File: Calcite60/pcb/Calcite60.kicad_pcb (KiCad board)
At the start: 2 copper layers, 226 x 94.8 mm, 176 parts, among them J1 USB_C_Receptacle_USB2.0, SW1 BOOT, SW2 RESET, U1 RT9013-33GB, U2 SRV05-4, U3 W25Q128JVS, U4 RP2040, Y1 12MHz

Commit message: Update BOM
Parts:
- renumbered H8 to H1, H3 to H10, H5 to H11, H1 to H12, H2 to H13, H14 to H2, H13 to H3, H12 to H4, H11 to H5, H9 to H6, H10 to H7, H4 to H8, H6 to H9

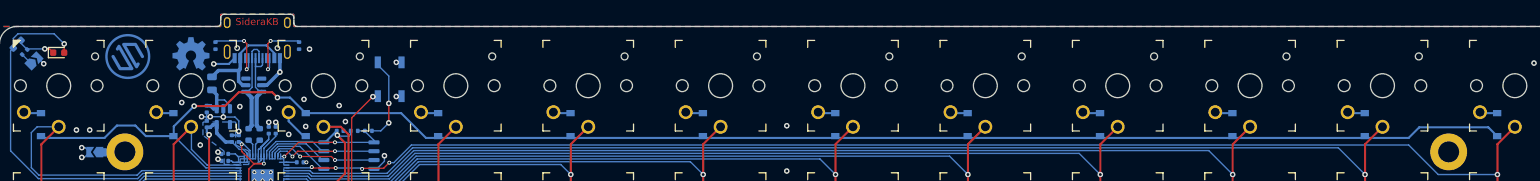
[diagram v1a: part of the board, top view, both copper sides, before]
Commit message: Reduce the size of the USB protrusion
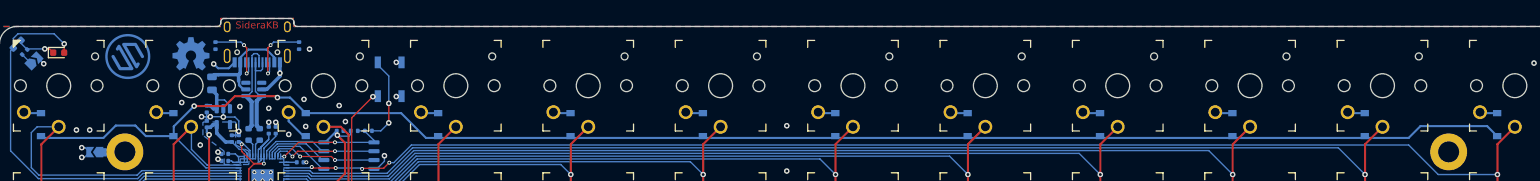
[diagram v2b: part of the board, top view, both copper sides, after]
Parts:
- moved J1 0.60 mm to (69.1, 50.5)
- moved U2 0.60 mm to (68.6, 58.4)
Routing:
- net /USB_D+: track 14.4 -> 13.8 mm
- net /USB_D-: track 14.3 -> 13.7 mm
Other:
- board size 226 x 94.8 mm -> 226 x 94.2 mm

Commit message: Update Calcite60 Rev2
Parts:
- removed C10, C11, C12, C13, C14, C15, C9: 100nF, Capacitor_SMD:C_0402_1005Metric
- removed C16, C8: 1uF, Capacitor_SMD:C_0402_1005Metric
- removed the SB1 at (37.1, 54.4)
- removed the U2 at (68.6, 58.4)
- added D1: 1N5819, Diode_SMD:D_SOD-323_HandSoldering, B.Cu at (43.7, 89.9)
- added H14: MountingHole, calcite:MountingWuerth_M2, B.Cu at (202.1, 67.4)
- added H15: MountingHole, calcite:MountingWuerth_M2, B.Cu at (240.1, 86.4)
- added H16: MountingHole, calcite:MountingWuerth_M2, B.Cu at (88.1, 67.4)
- added H17: MountingHole, calcite:MountingWuerth_M2, B.Cu at (50.1, 86.4)
- added H18: MountingHole, calcite:mouse_bite, F.Cu at (220.6, 123.7)
- added H19: MountingHole, calcite:mouse_bite, F.Cu at (220.6, 126.2)
- added H20: MountingHole, calcite:mouse_bite, F.Cu at (69.6, 123.7)
- added H21: MountingHole, calcite:mouse_bite, F.Cu at (69.6, 126.2)
- added H22: MountingHole, calcite:mouse_bite, F.Cu at (127.6, 123.7)
- added H23: MountingHole, calcite:mouse_bite, F.Cu at (127.6, 126.2)
- added H24: MountingHole, calcite:mouse_bite, F.Cu at (162.6, 123.7)
- added H25: MountingHole, calcite:mouse_bite, F.Cu at (162.6, 126.2)
- added J2: Conn_01x02, Connector_PinHeader_2.54mm:PinHeader_1x02_P2.54mm_Vertical, B.Cu at (150.6, 81.6)
- added J3: Conn_01x02, Connector_JST:JST_PH_S2B-PH-K_1x02_P2.00mm_Horizontal, B.Cu at (154.7, 81.9)
- added J4: Conn_01x02, Connector_PinHeader_2.54mm:PinHeader_1x02_P2.54mm_Vertical, B.Cu at (139.6, 84.2)
- added J5: Conn_01x02, Connector_JST:JST_PH_S2B-PH-K_1x02_P2.00mm_Horizontal, B.Cu at (135.6, 83.9)
- added J6: Conn_01x04, Connector_PinHeader_2.54mm:PinHeader_1x04_P2.54mm_Vertical, B.Cu at (110.1, 51.4)
- added J7: Conn_02x05_Counter_Clockwise, Connector_PinHeader_1.27mm:PinHeader_2x05_P1.27mm_Vertical, B.Cu at (122.1, 51.3)
- added KEY64: SW_Push_45deg, key-switches:SW_Kailh_Choc_V1_THT_nSilk, F.Cu at (126.1, 114.9)
- added KEY65: SW_Push_45deg, key-switches:SW_Kailh_Choc_V1_THT_nSilk, F.Cu at (145.1, 114.9)
- added KEY66: SW_Push_45deg, key-switches:SW_Kailh_Choc_V1_THT_nSilk, F.Cu at (164.1, 114.9)
- added LD1: Blue, LED_SMD:LED_0603_1608Metric, B.Cu at (61.6, 50.7)
- added Q1: AO3407, Package_TO_SOT_SMD:SOT-23, B.Cu at (43.6, 86.4)
- added R10: 820k, Resistor_SMD:R_0603_1608Metric, B.Cu at (60.6, 88.7)
- added U1: SRV05-4, Package_TO_SOT_SMD:SOT-23-6, B.Cu at (69.1, 58.9)
- C1: renamed from C3; value 100nF -> 1uF; footprint Capacitor_SMD:C_0402_1005Metric -> Capacitor_SMD:C_0603_1608Metric
- C2: renamed from C1; footprint Capacitor_SMD:C_0402_1005Metric -> Capacitor_SMD:C_0603_1608Metric
- C3: renamed from C2; footprint Capacitor_SMD:C_0402_1005Metric -> Capacitor_SMD:C_0603_1608Metric
- C4, C5: value 20pF -> 12pF; footprint Capacitor_SMD:C_0402_1005Metric -> Capacitor_SMD:C_0603_1608Metric
- C6, C7: value 100nF -> 10uF; footprint Capacitor_SMD:C_0402_1005Metric -> Capacitor_SMD:C_0603_1608Metric
- KEY1, KEY63: footprint key-switches:SW_Kailh_Choc_V1_THT -> key-switches:SW_Kailh_Choc_V1_THT_nSilk
- KEY10: renamed from KEY50; footprint key-switches:SW_Kailh_Choc_V1_THT -> key-switches:SW_Kailh_Choc_V1_THT_nSilk
- KEY11: renamed from KEY3; footprint key-switches:SW_Kailh_Choc_V1_THT -> key-switches:SW_Kailh_Choc_V1_THT_nSilk
- KEY12: renamed from KEY15; footprint key-switches:SW_Kailh_Choc_V1_THT -> key-switches:SW_Kailh_Choc_V1_THT_nSilk
- KEY13: renamed from KEY27; footprint key-switches:SW_Kailh_Choc_V1_THT -> key-switches:SW_Kailh_Choc_V1_THT_nSilk
- KEY14: renamed from KEY39; footprint key-switches:SW_Kailh_Choc_V1_THT -> key-switches:SW_Kailh_Choc_V1_THT_nSilk
- KEY15: renamed from KEY51; footprint key-switches:SW_Kailh_Choc_V1_THT -> key-switches:SW_Kailh_Choc_V1_THT_nSilk
- KEY16: renamed from KEY4; footprint key-switches:SW_Kailh_Choc_V1_THT -> key-switches:SW_Kailh_Choc_V1_THT_nSilk
- KEY17: renamed from KEY16; footprint key-switches:SW_Kailh_Choc_V1_THT -> key-switches:SW_Kailh_Choc_V1_THT_nSilk
- KEY18: renamed from KEY28; footprint key-switches:SW_Kailh_Choc_V1_THT -> key-switches:SW_Kailh_Choc_V1_THT_nSilk
- KEY19: renamed from KEY40; footprint key-switches:SW_Kailh_Choc_V1_THT -> key-switches:SW_Kailh_Choc_V1_THT_nSilk
- KEY2: renamed from KEY13; footprint key-switches:SW_Kailh_Choc_V1_THT -> key-switches:SW_Kailh_Choc_V1_THT_nSilk
- KEY20: renamed from KEY52; footprint key-switches:SW_Kailh_Choc_V1_THT -> key-switches:SW_Kailh_Choc_V1_THT_nSilk
- KEY21: renamed from KEY53; footprint key-switches:SW_Kailh_Choc_V1_THT -> key-switches:SW_Kailh_Choc_V1_THT_nSilk
- KEY22: renamed from KEY5; footprint key-switches:SW_Kailh_Choc_V1_THT -> key-switches:SW_Kailh_Choc_V1_THT_nSilk
- KEY23: renamed from KEY17; footprint key-switches:SW_Kailh_Choc_V1_THT -> key-switches:SW_Kailh_Choc_V1_THT_nSilk
- KEY24: renamed from KEY29; footprint key-switches:SW_Kailh_Choc_V1_THT -> key-switches:SW_Kailh_Choc_V1_THT_nSilk
- KEY25: renamed from KEY41; footprint key-switches:SW_Kailh_Choc_V1_THT -> key-switches:SW_Kailh_Choc_V1_THT_nSilk
- KEY26: renamed from KEY54; footprint key-switches:SW_Kailh_Choc_V1_THT -> key-switches:SW_Kailh_Choc_V1_THT_nSilk
- KEY27: renamed from KEY6; footprint key-switches:SW_Kailh_Choc_V1_THT -> key-switches:SW_Kailh_Choc_V1_THT_nSilk
- KEY28: renamed from KEY18; footprint key-switches:SW_Kailh_Choc_V1_THT -> key-switches:SW_Kailh_Choc_V1_THT_nSilk
- KEY29: renamed from KEY30; footprint key-switches:SW_Kailh_Choc_V1_THT -> key-switches:SW_Kailh_Choc_V1_THT_nSilk
- KEY3: renamed from KEY25; footprint key-switches:SW_Kailh_Choc_V1_THT -> key-switches:SW_Kailh_Choc_V1_THT_nSilk
- KEY30: renamed from KEY42; footprint key-switches:SW_Kailh_Choc_V1_THT -> key-switches:SW_Kailh_Choc_V1_THT_nSilk
- KEY31: renamed from KEY55; footprint key-switches:SW_Kailh_Choc_V1_THT -> key-switches:SW_Kailh_Choc_V1_THT_nSilk
- KEY32: renamed from KEY56; footprint key-switches:SW_Kailh_Choc_V1_THT -> key-switches:SW_Kailh_Choc_V1_THT_nSilk
- KEY33: renamed from KEY7; footprint key-switches:SW_Kailh_Choc_V1_THT -> key-switches:SW_Kailh_Choc_V1_THT_nSilk
- KEY34: renamed from KEY19; footprint key-switches:SW_Kailh_Choc_V1_THT -> key-switches:SW_Kailh_Choc_V1_THT_nSilk
- KEY35: renamed from KEY31; footprint key-switches:SW_Kailh_Choc_V1_THT -> key-switches:SW_Kailh_Choc_V1_THT_nSilk
- KEY36: renamed from KEY43; footprint key-switches:SW_Kailh_Choc_V1_THT -> key-switches:SW_Kailh_Choc_V1_THT_nSilk
- KEY37: renamed from KEY57; footprint key-switches:SW_Kailh_Choc_V1_THT -> key-switches:SW_Kailh_Choc_V1_THT_nSilk
- KEY38: renamed from KEY58; footprint key-switches:SW_Kailh_Choc_V1_THT -> key-switches:SW_Kailh_Choc_V1_THT_nSilk
- KEY39: renamed from KEY8; footprint key-switches:SW_Kailh_Choc_V1_THT -> key-switches:SW_Kailh_Choc_V1_THT_nSilk
- KEY4: renamed from KEY37; footprint key-switches:SW_Kailh_Choc_V1_THT -> key-switches:SW_Kailh_Choc_V1_THT_nSilk
- KEY40: renamed from KEY20; footprint key-switches:SW_Kailh_Choc_V1_THT -> key-switches:SW_Kailh_Choc_V1_THT_nSilk
- KEY41: renamed from KEY32; footprint key-switches:SW_Kailh_Choc_V1_THT -> key-switches:SW_Kailh_Choc_V1_THT_nSilk
- KEY42: renamed from KEY44; footprint key-switches:SW_Kailh_Choc_V1_THT -> key-switches:SW_Kailh_Choc_V1_THT_nSilk
- KEY43: renamed from KEY59; footprint key-switches:SW_Kailh_Choc_V1_THT -> key-switches:SW_Kailh_Choc_V1_THT_nSilk
- KEY44: renamed from KEY9; footprint key-switches:SW_Kailh_Choc_V1_THT -> key-switches:SW_Kailh_Choc_V1_THT_nSilk
- KEY45: renamed from KEY21; footprint key-switches:SW_Kailh_Choc_V1_THT -> key-switches:SW_Kailh_Choc_V1_THT_nSilk
- KEY46: renamed from KEY33; footprint key-switches:SW_Kailh_Choc_V1_THT -> key-switches:SW_Kailh_Choc_V1_THT_nSilk
- KEY47: renamed from KEY45; footprint key-switches:SW_Kailh_Choc_V1_THT -> key-switches:SW_Kailh_Choc_V1_THT_nSilk
- KEY48: renamed from KEY60; footprint key-switches:SW_Kailh_Choc_V1_THT -> key-switches:SW_Kailh_Choc_V1_THT_nSilk
- KEY49: renamed from KEY10; footprint key-switches:SW_Kailh_Choc_V1_THT -> key-switches:SW_Kailh_Choc_V1_THT_nSilk
- KEY5: renamed from KEY49; footprint key-switches:SW_Kailh_Choc_V1_THT -> key-switches:SW_Kailh_Choc_V1_THT_nSilk
- KEY50: renamed from KEY22; footprint key-switches:SW_Kailh_Choc_V1_THT -> key-switches:SW_Kailh_Choc_V1_THT_nSilk
- KEY51: renamed from KEY34; footprint key-switches:SW_Kailh_Choc_V1_THT -> key-switches:SW_Kailh_Choc_V1_THT_nSilk
- KEY52: renamed from KEY46; footprint key-switches:SW_Kailh_Choc_V1_THT -> key-switches:SW_Kailh_Choc_V1_THT_nSilk
- KEY53: renamed from KEY61; footprint key-switches:SW_Kailh_Choc_V1_THT -> key-switches:SW_Kailh_Choc_V1_THT_nSilk
- KEY54: renamed from KEY11; footprint key-switches:SW_Kailh_Choc_V1_THT -> key-switches:SW_Kailh_Choc_V1_THT_nSilk
- KEY55: renamed from KEY23; footprint key-switches:SW_Kailh_Choc_V1_THT -> key-switches:SW_Kailh_Choc_V1_THT_nSilk
- KEY56: renamed from KEY35; footprint key-switches:SW_Kailh_Choc_V1_THT -> key-switches:SW_Kailh_Choc_V1_THT_nSilk
- KEY57: renamed from KEY47; footprint key-switches:SW_Kailh_Choc_V1_THT -> key-switches:SW_Kailh_Choc_V1_THT_nSilk
- KEY58: renamed from KEY62; footprint key-switches:SW_Kailh_Choc_V1_THT -> key-switches:SW_Kailh_Choc_V1_THT_nSilk
- KEY59: renamed from KEY12; footprint key-switches:SW_Kailh_Choc_V1_THT -> key-switches:SW_Kailh_Choc_V1_THT_nSilk
- KEY6: renamed from KEY2; footprint key-switches:SW_Kailh_Choc_V1_THT -> key-switches:SW_Kailh_Choc_V1_THT_nSilk
- KEY60: renamed from KEY24; footprint key-switches:SW_Kailh_Choc_V1_THT -> key-switches:SW_Kailh_Choc_V1_THT_nSilk
- KEY61: renamed from KEY36; footprint key-switches:SW_Kailh_Choc_V1_THT -> key-switches:SW_Kailh_Choc_V1_THT_nSilk
- KEY62: renamed from KEY48; footprint key-switches:SW_Kailh_Choc_V1_THT -> key-switches:SW_Kailh_Choc_V1_THT_nSilk
- KEY7: renamed from KEY14; footprint key-switches:SW_Kailh_Choc_V1_THT -> key-switches:SW_Kailh_Choc_V1_THT_nSilk
- KEY8: renamed from KEY26; footprint key-switches:SW_Kailh_Choc_V1_THT -> key-switches:SW_Kailh_Choc_V1_THT_nSilk
- KEY9: renamed from KEY38; footprint key-switches:SW_Kailh_Choc_V1_THT -> key-switches:SW_Kailh_Choc_V1_THT_nSilk
- LD2: renamed from LD1; moved to F.Cu
- R1, R2, R7, R8: footprint Resistor_SMD:R_0402_1005Metric -> Resistor_SMD:R_0603_1608Metric
- R3: renamed from R4; value 27 -> 1k
- R4: renamed from R5; value 27 -> 5.1k
- R5: renamed from R6; value 1k -> 100k; footprint Resistor_SMD:R_0402_1005Metric -> Resistor_SMD:R_0603_1608Metric
- R6: renamed from R3; footprint Resistor_SMD:R_0402_1005Metric -> Resistor_SMD:R_0603_1608Metric
- R9: value 10k -> 2M; footprint Resistor_SMD:R_0402_1005Metric -> Resistor_SMD:R_0603_1608Metric
- SW1: value BOOT -> SW_DPDT_x2; footprint Button_Switch_SMD:SW_SPST_B3U-1000P -> calcite:9_3.5_3.5 Switch
- U2: renamed from U3; value W25Q128JVS -> TP4054; footprint Package_SO:SOIC-8_5.23x5.23mm_P1.27mm -> Package_TO_SOT_SMD:SOT-23-5
- U4: value RP2040 -> E73-2G4M08S1C; footprint Package_DFN_QFN:QFN-56-1EP_7x7mm_P0.4mm_EP3.2x3.2mm -> calcite:E73-2G4M08S1C-52840
- Y1: value 12MHz -> 32.768kHz; footprint Crystal:Crystal_SMD_3225-4Pin_3.2x2.5mm -> Crystal:Crystal_SMD_3215-2Pin_3.2x1.5mm
- moved G*** 77.8 mm to (143.8, 35.2)
- moved H7 68.5 mm to (183.1, 124.4)
- moved H9 68.5 mm to (107.1, 124.4)
- moved C1 49.5 mm to (38.6, 89.9), turned to 180 degrees
- moved U2 47.4 mm to (38.6, 86.4), turned to -90 degrees
- moved R5 45.3 mm to (43.7, 82.9)
- moved R4 38.8 mm to (35.6, 86.4), turned to 90 degrees
- moved R8 35.8 mm to (43.9, 53.2), turned to -90 degrees
- moved R3 35.7 mm to (38.6, 82.9), turned to 180 degrees
- moved R7 27.5 mm to (60.6, 80.4)
- moved C2 26.8 mm to (56.1, 87.4), turned to 180 degrees
- moved C6 23.6 mm to (60.6, 85.2), turned to 180 degrees
- moved U3 23.0 mm to (56.1, 83.9), turned to 90 degrees
- moved G*** 20.5 mm to (45.0, 34.0)
- moved C4 18.4 mm to (57.6, 92.9)
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- renumbered D38 to D10, D50 to D11, D3 to D12, D15 to D13, D27 to D14, D39 to D15, D51 to D16, D4 to D17, D16 to D18, D28 to D19, D1 to D2, D40 to D20, D52 to D21, D5 to D22, D17 to D23, D29 to D24, D41 to D25, D53 to D26, D6 to D27, D18 to D28, D30 to D29, D13 to D3, D42 to D30, D54 to D31, D7 to D32, D19 to D33, D31 to D34, D43 to D35, D55 to D36, D8 to D37, D20 to D38, D32 to D39, D25 to D4, D44 to D40, D56 to D41, D9 to D42, D21 to D43, D33 to D44, D57 to D46, D10 to D47, D22 to D48, D34 to D49, D37 to D5, D46 to D50, D58 to D51, D11 to D52, D23 to D53, D35 to D54, D47 to D55, D59 to D56, D12 to D57, D24 to D58, D36 to D59, D49 to D6, D48 to D60, D60 to D61, D2 to D7, D14 to D8, D26 to D9, H6 to H10, H7 to H12, H9 to H13, H12 to H3, H3 to H4, H13 to H5, H4 to H6, H10 to H7, H5 to H8, H8 to H9, LD2 to LD3, SB2 to SB1, U1 to U3
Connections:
- C1 pad 1: +3V3 -> +5V
- C2 pad 1: +5V -> Net-(D1-K)
- C3 pad 1: +3V3 -> VDD
- C4 pad 1: GND -> Net-(U4-P0.00/XL1)
- C4 pad 2: Net-(U4-XIN) -> GND
- C5 pad 2: Net-(C5-Pad2) -> Net-(U4-P0.01/XL2)
- C6 pad 1: +1V1 -> VDD
- C7 pad 1: +1V1 -> +5V
- D31 pad 2: Net-(D54-A) (its old number) -> Net-(D31-A)
- D36 pad 2: Net-(D55-A) (its old number) -> Net-(D36-A)
- D41 pad 2: Net-(D56-A) (its old number) -> Net-(D41-A)
- J1 pad A6: /USB_D+ -> USB_D+
- J1 pad A7: /USB_D- -> USB_D-
- J1 pad B6: /USB_D+ -> USB_D+
- J1 pad B7: /USB_D- -> USB_D-
- KEY26 pad 1: COL_5 -> Net-(D31-A)
- KEY26 pad 2: Net-(D54-A) (its old number) -> COL_5
- KEY31 pad 1: Net-(D54-A) (its old number) -> COL_5
- KEY31 pad 2: COL_5 -> Net-(D31-A)
- KEY32 pad 1: COL_6 -> Net-(D36-A)
- KEY32 pad 2: Net-(D55-A) (its old number) -> COL_6
- KEY37 pad 1: Net-(D55-A) (its old number) -> COL_6
- KEY37 pad 2: COL_6 -> Net-(D36-A)
- KEY38 pad 1: COL_7 -> Net-(D41-A)
- KEY38 pad 2: Net-(D56-A) (its old number) -> COL_7
- KEY43 pad 1: Net-(D56-A) (its old number) -> COL_7
- KEY43 pad 2: COL_7 -> Net-(D41-A)
- LD2 pad 1: Net-(LD1-K) -> Net-(LD2-K)
- LD2 pad 2: STATE_LED -> State_LED_1
- LD3 pad 1: Net-(LD1-K) -> Net-(LD3-K)
- LD3 pad 2: STATE_LED -> State_LED_2
- R3 pad 1: /USB_D+ -> Net-(LD1-K)
- R3 pad 2: Net-(U4-USB_DP) -> Net-(U2-~{CHRG})
- R4 pad 1: /USB_D- -> Net-(U2-PROG)
- R4 pad 2: Net-(U4-USB_DM) -> GND
- R5 pad 1: /RP2040/BOOT -> +5V
- R5 pad 2: /RP2040/QSPI_SS -> GND
- R6 pad 1: Net-(LD1-K) -> Net-(LD2-K)
- R6 pad 2: Net-(SB1-A) (its old number) -> GND
- R7 pad 1: +3V3 -> VDD
- R7 pad 2: /RP2040/QSPI_SS -> ~{RESET}
- R8 pad 1: Net-(C5-Pad2) -> Net-(LD3-K)
- R8 pad 2: Net-(U4-XOUT) -> GND
- R9 pad 1: +3V3 -> Battery_sense
- R9 pad 2: /RP2040/~{RESET} -> GND
- SW1 pad 1: GND -> +BATT
- SW1 pad 2: /RP2040/BOOT -> Net-(Q1-D)
- SW2 pad 2: /RP2040/~{RESET} -> ~{RESET}
- U2 pad 1: /RP2040/QSPI_SS -> Net-(U2-~{CHRG})
- U2 pad 2: /RP2040/QSPI_D1 -> GND
- U2 pad 3: /RP2040/QSPI_D2 -> +BATT
- U2 pad 4: GND -> +5V
- U2 pad 5: /RP2040/QSPI_D0 -> Net-(U2-PROG)
- U3 pad 1: +5V -> Net-(D1-K)
- U3 pad 3: +5V -> Net-(D1-K)
- U3 pad 5: +3V3 -> VDD
- U4 pad 1: +3V3 -> State_LED_1
- U4 pad 10: +3V3 -> COL_0
- U4 pad 11: unconnected-(U4-GPIO8-Pad11) -> Net-(U4-P0.00/XL1)
- U4 pad 12: COL_5 -> unconnected-(U4-P0.26-Pad12)
- U4 pad 13: COL_4 -> Net-(U4-P0.01/XL2)
- U4 pad 14: COL_3 -> unconnected-(U4-P0.06-Pad14)
- U4 pad 15: COL_2 -> unconnected-(U4-P0.05-Pad15)
- U4 pad 18: unconnected-(U4-GPIO15-Pad18) -> Battery_sense
- U4 pad 19: GND -> VDD
- U4 pad 2: unconnected-(U4-GPIO0-Pad2) -> State_LED_2
- U4 pad 20: Net-(U4-XIN) -> unconnected-(U4-P0.12-Pad20)
- U4 pad 21: Net-(U4-XOUT) -> GND
- U4 pad 22: +3V3 -> unconnected-(U4-P0.07-Pad22)
- U4 pad 23: +1V1 -> VDD
- U4 pad 24: unconnected-(U4-SWCLK-Pad24) -> GND
- U4 pad 25: unconnected-(U4-SWD-Pad25) -> /MCU/DCCH
- U4 pad 26: /RP2040/~{RESET} -> ~{RESET}
- U4 pad 27: unconnected-(U4-GPIO16-Pad27) -> +5V
- U4 pad 28: unconnected-(U4-GPIO17-Pad28) -> ROW_0
- U4 pad 29: ROW_1 -> USB_D-
- U4 pad 3: COL_11 -> COL_7
- U4 pad 31: unconnected-(U4-GPIO20-Pad31) -> USB_D+
- U4 pad 32: unconnected-(U4-GPIO21-Pad32) -> ROW_3
- U4 pad 33: +3V3 -> unconnected-(U4-P0.13-Pad33)
- U4 pad 34: unconnected-(U4-GPIO22-Pad34) -> ROW_4
- U4 pad 36: ROW_3 -> COL_8
- U4 pad 37: ROW_4 -> SWD
- U4 pad 38: STATE_LED -> COL_9
- U4 pad 39: COL_0 -> SWC
- U4 pad 4: COL_10 -> COL_6
- U4 pad 40: ROW_0 -> COL_10
- U4 pad 41: COL_1 -> COL_2
- U4 pad 42: +3V3 -> COL_11
- U4 pad 43: +3V3 -> ROW_1
- U4 pad 5: COL_9 -> GND
- U4 pad 6: COL_8 -> COL_5
- U4 pad 7: COL_7 -> COL_4
- U4 pad 8: COL_6 -> COL_3
- U4 pad 9: unconnected-(U4-GPIO7-Pad9) -> COL_1
- Y1 pad 1: Net-(C5-Pad2) -> Net-(U4-P0.01/XL2)
- Y1 pad 2: GND -> Net-(U4-P0.00/XL1)
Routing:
- net +BATT: track 0.00 -> 218.8 mm
- net COL_10: track 243.6 -> 93.5 mm, vias 1 -> 0
- net COL_11: track 262.7 -> 129.1 mm, vias 5 -> 0
- net COL_9: track 224.5 -> 94.6 mm, vias 1 -> 0
- net ~{RESET}: track 0.00 -> 90.0 mm, vias 0 -> 2
- net +3V3: track 88.3 -> 0.00 mm, vias 3 -> 0
- net ROW_3: track 296.0 -> 209.0 mm
- net Net-(Q1-D): track 0.00 -> 85.8 mm, vias 0 -> 2
- net ROW_4: track 313.1 -> 227.9 mm
- net COL_7: track 188.2 -> 109.1 mm, vias 1 -> 0
- net SWC: track 0.00 -> 71.9 mm, vias 0 -> 1
- net SWD: track 0.00 -> 70.4 mm, vias 0 -> 1
- net +5V: track 7.27 -> 74.2 mm, vias 0 -> 2
- net ROW_2: track 273.4 -> 210.1 mm
- net COL_3: track 114.3 -> 176.2 mm
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- removed copper zone on B.Cu, net +3V3
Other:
- outline, holes or cut-outs redrawn
- board text added: "locked"
- board text removed: "SideraKB"
